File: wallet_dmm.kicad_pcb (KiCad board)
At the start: 2 copper layers, 86 x 53 mm, 26 parts, among them J1 Conn_01x04, J2 Conn_01x02, Q1 T2N7002BK_LM, Q2 T2N7002BK_LM, SW1 RESET_BUTTON, SW2 BUTTON0, SW3 BUTTON1, SW4 BUTTON2, U1 STM32L051K8Tx, U2 TLC555xD, U3 MCP9700-E/TO

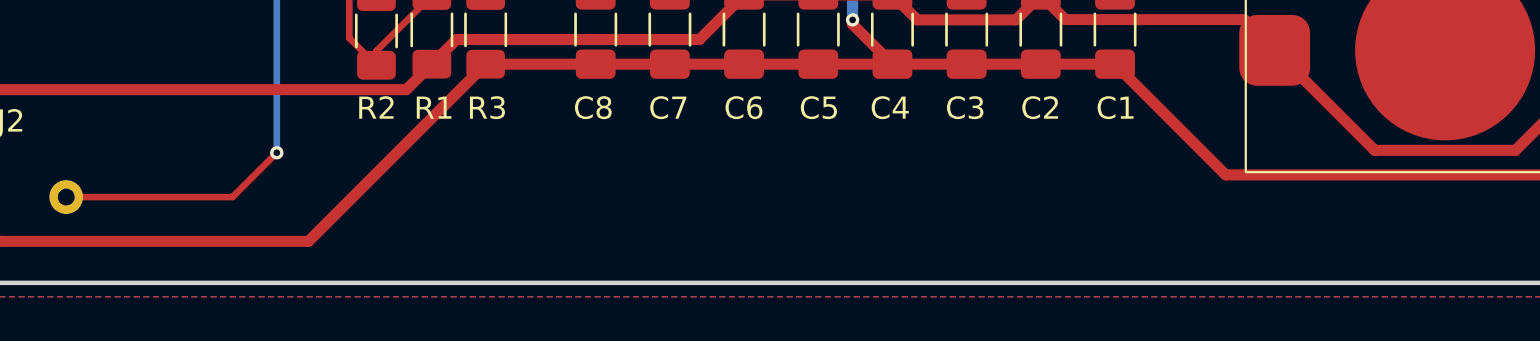
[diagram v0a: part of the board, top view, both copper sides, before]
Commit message: Added silkscreen signature and revision number.
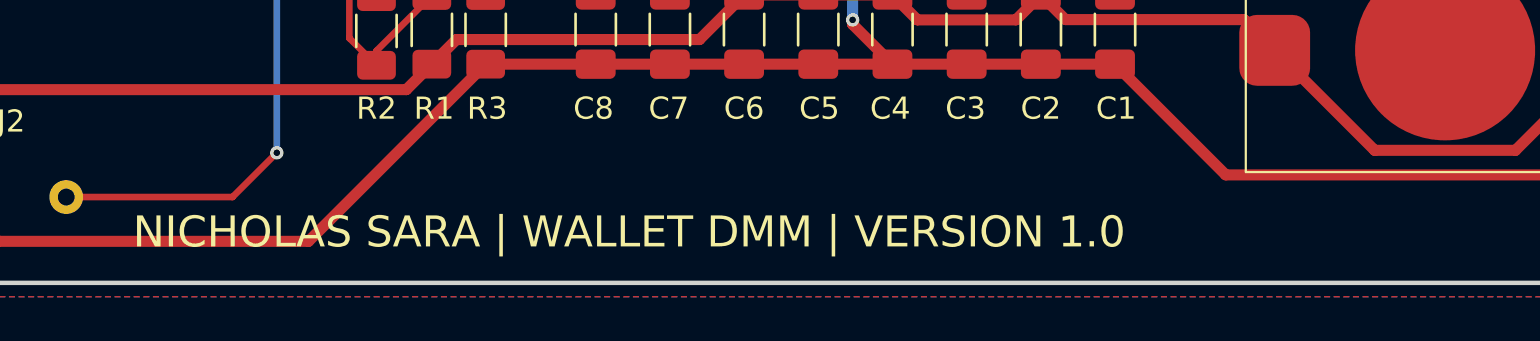
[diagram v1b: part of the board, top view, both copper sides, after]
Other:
- board text added: "NICHOLAS SARA | WALLET DMM | VERSION 1.0"
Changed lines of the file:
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@@
 		(layer "Edge.Cuts")
+	)
+	(gr_text "NICHOLAS SARA | WALLET DMM | VERSION 1.0\n"
+		(at 86 80.4 0)
+		(layer "F.SilkS")
+		(effects
+			(font
+				(size 1.4 1.4)
+				(thickness 0.1)
+			)
+			(justify left bottom)
+		)
 	)
 	(segment
